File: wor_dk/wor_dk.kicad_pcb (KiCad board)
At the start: 4 copper layers, 108.7 x 57.5 mm, 139 parts, among them J101 Conn_01x02, J102 Conn_02x03_Odd_Even, J103 Conn_02x03_Odd_Even, J104 Conn_01x02, J201 SWD, J301 SMA, J302 Conn_02x04_Odd_Even, J303 Conn_02x06_Odd_Even, J401 USB_C_Receptacle_USB2.0_16P, J501 SWD, J502 USB_C_Receptacle_USB2.0_16P, J503 SWD, Q501 BSS84, SW201 SW_Push, SW501 SW_Push, U201 nRF52840, U202 TMUX1112PWR, U203 TMUX1112PWR, U301 Si4467, U401 FT232RL, U501 TLV1117-33, U502 LPC11U35FHI33_501, Y201 32.768kHz, Y202 32MHz, Y301 26MHz, Y501 12MHz

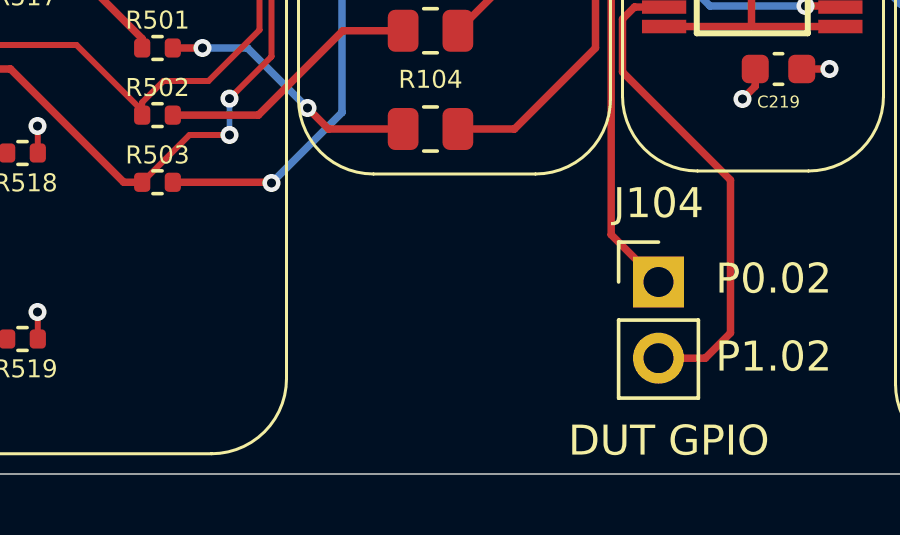
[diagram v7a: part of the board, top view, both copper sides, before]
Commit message: wor_dk: PCB: add smart tulip logo
This also requires the logos library to be added, so that we don't get
a DRC warning.
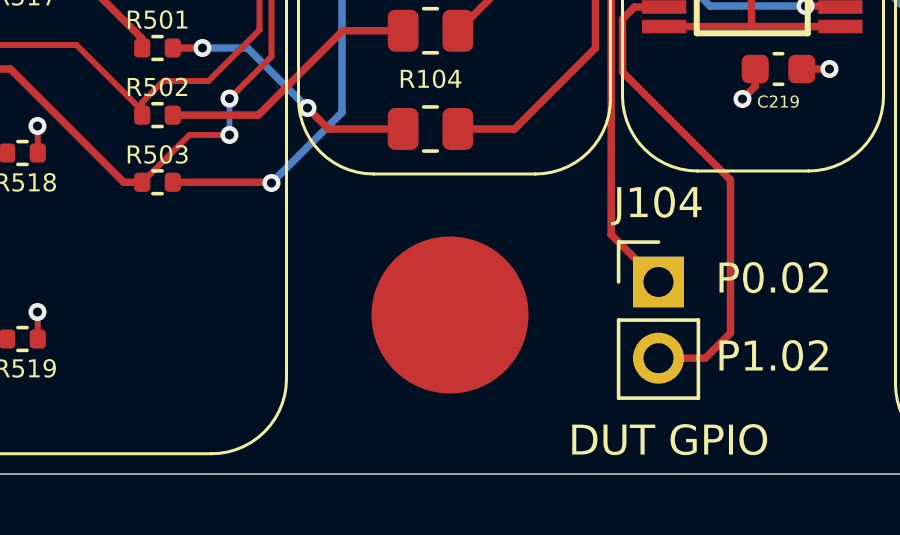
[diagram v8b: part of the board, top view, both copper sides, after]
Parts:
- added G1: smart logo, Logos:smart_tulip_soldermask, F.Cu at (102.1, 106.8)
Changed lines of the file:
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@@
 		)
 	)
+	(footprint "Logos:smart_tulip_soldermask"
+		(layer "F.Cu")
+		(at 102.13 106.85)
+		(property "Reference" "G1"
+			(at -1.016 -3.302 0)
+			(layer "F.SilkS")
+			(hide yes)
+			(effects
+				(font
+					(size 0.4 0.4)
+					(thickness 0.1)
+				)
+			)
+		)
+		(property "Value" "smart logo"
+			(at 0.254 3.556 0)
+			(layer "F.SilkS")
+			(hide yes)
+			(effects
+				(font
+					(size 1.524 1.524)
+					(thickness 0.3)
+				)
+			)
+		)
+		(property "Footprint" "Logos:smart_tulip_soldermask"
+			(at 0 0 0)
+			(unlocked yes)
+			(layer "F.Fab")
+			(hide yes)
+			(effects
+				(font
+					(size 1.27 1.27)
+					(thickness 0.15)
+				)
+			)
+		)
+		(property "Datasheet" ""
+			(at 0 0 0)
+			(unlocked yes)
+			(layer "F.Fab")
+			(hide yes)
+			(effects
+				(font
+					(size 1.27 1.27)
+					(thickness 0.15)
+				)
+			)
+		)
+		(property "Description" ""
+			(at 0 0 0)
+			(unlocked yes)
+			(layer "F.Fab")
+			(hide yes)
+			(effects
+				(font
+					(size 1.27 1.27)
+					(thickness 0.15)
+				)
+			)
+		)
+		(attr through_hole board_only)
+		(fp_poly
+			(pts
+				(xy 1.422426 -0.378883) (xy 1.420006 -0.317863) (xy 1.413171 -0.245699) (xy 1.40263 -0.167389) (xy 1.389089 -0.087929)
+				(xy 1.373258 -0.012316) (xy 1.36666 0.014876) (xy 1.315718 0.182018) (xy 1.249879 0.341973) (xy 1.169932 0.493942)
+				(xy 1.076662 0.637125) (xy 0.970857 0.770722) (xy 0.853303 0.893933) (xy 0.724786 1.005959) (xy 0.586095 1.105999)
+				(xy 0.438015 1.193254) (xy 0.281333 1.266924) (xy 0.116836 1.326208) (xy 0.060618 1.342576) (xy -0.004628 1.358579)
+				(xy -0.077678 1.37333) (xy -0.15378 1.386112) (xy -0.22818 1.396206) (xy -0.296128 1.402895) (xy -0.35287 1.40546)
+				(xy -0.355534 1.405467) (xy -0.423333 1.405467) (xy -0.423333 1.120269) (xy -0.309799 1.110728)
+				(xy -0.144538 1.08871) (xy 0.014273 1.051181) (xy 0.166026 0.998503) (xy 0.310111 0.931038) (xy 0.44592 0.849149)
+				(xy 0.572844 0.753198) (xy 0.690273 0.643547) (xy 0.797599 0.520558) (xy 0.883927 0.400481) (xy 0.949311 0.289348)
+				(xy 1.006427 0.169348) (xy 1.053931 0.044301) (xy 1.090479 -0.081973) (xy 1.114728 -0.205651) (xy 1.123001 -0.2794)
+				(xy 1.125741 -0.31275) (xy 1.1284 -0.341175) (xy 1.130439 -0.358949) (xy 1.130574 -0.359833) (xy 1.132569 -0.379718)
+				(xy 1.13384 -0.405692) (xy 1.133905 -0.408516) (xy 1.134534 -0.440266) (xy 1.4224 -0.440266) (xy 1.422426 -0.378883)
+			)
+			(stroke
+				(width 0.01)
+				(type solid)
+			)
+			(fill solid)
+			(layer "F.Mask")
+		)
+		(fp_poly
+			(pts
+				(xy -1.85349 -2.027975) (xy -1.769722 -2.016646) (xy -1.682248 -1.999131) (xy -1.596562 -1.976547)
+				(xy -1.518155 -1.950012) (xy -1.510575 -1.947045) (xy -1.379298 -1.886043) (xy -1.256531 -1.811061)
+				(xy -1.143543 -1.723118) (xy -1.041596 -1.623235) (xy -0.951959 -1.512431) (xy -0.927803 -1.477433)
+				(xy -0.871278 -1.384506) (xy -0.823907 -1.288617) (xy -0.783743 -1.185302) (xy -0.748837 -1.070095)
+				(xy -0.746831 -1.062566) (xy -0.724422 -0.977899) (xy -0.721751 -0.08255) (xy -0.71908 0.812801)
+				(xy -0.768056 0.811532) (xy -0.800202 0.810232) (xy -0.82942 0.808279) (xy -0.842433 0.806954) (xy -0.990098 0.780992)
+				(xy -1.126779 0.742744) (xy -1.253726 0.691629) (xy -1.372188 0.62707) (xy -1.483415 0.548485) (xy -1.577133 0.466475)
+				(xy -1.674185 0.364294) (xy -1.755806 0.258166) (xy -1.823403 0.145898) (xy -1.878387 0.025297)
+				(xy -1.901206 -0.037666) (xy -1.912127 -0.070833) (xy -1.921877 -0.102169) (xy -1.930522 -0.132787)
+				(xy -1.938128 -0.163801) (xy -1.944761 -0.196327) (xy -1.950489 -0.231477) (xy -1.955377 -0.270367)
+				(xy -1.959492 -0.31411) (xy -1.9629 -0.363821) (xy -1.965667 -0.420613) (xy -1.96786 -0.4856) (xy -1.969545 -0.559898)
+				(xy -1.970788 -0.64462) (xy -1.971656 -0.74088) (xy -1.972216 -0.849793) (xy -1.972533 -0.972472)
+				(xy -1.972673 -1.110032) (xy -1.972704 -1.238249) (xy -1.972733 -2.031999) (xy -1.928061 -2.031999)
+				(xy -1.85349 -2.027975)
+			)
+			(stroke
+				(width 0.01)
+				(type solid)
+			)
+			(fill solid)
+			(layer "F.Mask")
+		)
+		(fp_poly
+			(pts
+				(xy 2.014986 -0.366183) (xy 2.013367 -0.31459) (xy 2.008961 -0.251486) (xy 2.002299 -0.181965) (xy 1.993912 -0.111119)
+				(xy 1.984331 -0.044044) (xy 1.976816 0) (xy 1.935403 0.181311) (xy 1.879264 0.361862) (xy 1.809646 0.538651)
+				(xy 1.727793 0.708674) (xy 1.634954 0.868926) (xy 1.585094 0.944034) (xy 1.470967 1.094835) (xy 1.343369 1.238976)
+				(xy 1.205012 1.373744) (xy 1.058608 1.496427) (xy 0.960967 1.568023) (xy 0.79508 1.672971) (xy 0.620613 1.76425)
+				(xy 0.439187 1.841309) (xy 0.252427 1.9036) (xy 0.061957 1.950573) (xy -0.130601 1.981678) (xy -0.30198 1.995552)
+				(xy -0.423333 2.00071) (xy -0.423333 1.710267) (xy -0.38735 1.709061) (xy -0.355963 1.707714) (xy -0.325689 1.705975)
+				(xy -0.321733 1.705697) (xy -0.298943 1.70403) (xy -0.265806 1.701596) (xy -0.22886 1.698876) (xy -0.222757 1.698426)
+				(xy -0.163102 1.692069) (xy -0.092387 1.681375) (xy -0.015635 1.667305) (xy 0.062131 1.650822) (xy 0.135888 1.632889)
+				(xy 0.174258 1.622373) (xy 0.35114 1.562729) (xy 0.521412 1.487915) (xy 0.684146 1.398713) (xy 0.838412 1.295908)
+				(xy 0.983279 1.180282) (xy 1.117817 1.052617) (xy 1.241096 0.913697) (xy 1.352187 0.764304) (xy 1.450159 0.605221)
+				(xy 1.503078 0.503767) (xy 1.54518 0.414252) (xy 1.57972 0.333112) (xy 1.608782 0.254802) (xy 1.634449 0.17378)
+				(xy 1.654635 0.100626) (xy 1.674989 0.012869) (xy 1.69305 -0.084114) (xy 1.70803 -0.184701) (xy 1.719138 -0.283274)
+				(xy 1.725584 -0.37421) (xy 1.726779 -0.412749) (xy 1.7272 -0.440266) (xy 2.015067 -0.440266) (xy 2.014986 -0.366183)
+			)
+			(stroke
+				(width 0.01)
+				(type solid)
+			)
+			(fill solid)
+			(layer "F.Mask")
+		)
+		(fp_poly
+			(pts
+				(xy 0.82913 -1.197212) (xy 0.828938 -1.051014) (xy 0.828674 -0.920675) (xy 0.828303 -0.805123) (xy 0.827792 -0.703284)
+				(xy 0.827106 -0.614085) (xy 0.826211 -0.536453) (xy 0.825073 -0.469313) (xy 0.823656 -0.411592)
+				(xy 0.821928 -0.362218) (xy 0.819853 -0.320117) (xy 0.817398 -0.284215) (xy 0.814527 -0.253439)
+				(xy 0.811207 -0.226716) (xy 0.807404 -0.202971) (xy 0.803082 -0.181133) (xy 0.798209 -0.160127)
+				(xy 0.795662 -0.150022) (xy 0.751166 -0.008914) (xy 0.692897 0.123628) (xy 0.621745 0.24685) (xy 0.538601 0.359998)
+				(xy 0.444358 0.46232) (xy 0.339904 0.553059) (xy 0.226133 0.631464) (xy 0.103934 0.696779) (xy -0.0258 0.748252)
+				(xy -0.16218 0.785127) (xy -0.304314 0.806652) (xy -0.338272 0.809389) (xy -0.423996 0.815157) (xy -0.421494 0.054617)
+				(xy -0.145595 0.054617) (xy -0.142333 0.117536) (xy -0.12428 0.17979) (xy -0.101945 0.222459) (xy -0.066009 0.265527)
+				(xy -0.017982 0.303008) (xy 0.037405 0.331249) (xy 0.040617 0.33248) (xy 0.085559 0.342776) (xy 0.13803 0.344634)
+				(xy 0.191058 0.338358) (xy 0.237669 0.324251) (xy 0.238555 0.323862) (xy 0.288476 0.293885) (xy 0.333949 0.252032)
+				(xy 0.369809 0.203341) (xy 0.378249 0.187477) (xy 0.395458 0.136568) (xy 0.402768 0.079669) (xy 0.400029 0.022884)
+				(xy 0.387087 -0.027682) (xy 0.383801 -0.035354) (xy 0.355383 -0.082238) (xy 0.316327 -0.126594)
+				(xy 0.272052 -0.162732) (xy 0.250107 -0.17571) (xy 0.196331 -0.194824) (xy 0.136072 -0.202465) (xy 0.075585 -0.198312)
+				(xy 0.032622 -0.186812) (xy -0.026355 -0.156201) (xy -0.074446 -0.114376) (xy -0.110871 -0.063715)
+				(xy -0.134847 -0.006592) (xy -0.145595 0.054617) (xy -0.421494 0.054617) (xy -0.421074 -0.072905)
+				(xy -0.420619 -0.217041) (xy -0.420218 -0.345333) (xy -0.419813 -0.45887) (xy -0.419347 -0.558742)
+				(xy -0.418762 -0.646038) (xy -0.418 -0.721847) (xy -0.417003 -0.787257) (xy -0.415713 -0.843359)
+				(xy -0.414074 -0.891241) (xy -0.412026 -0.931993) (xy -0.409513 -0.966703) (xy -0.406476 -0.996461)
+				(xy -0.402858 -1.022356) (xy -0.398601 -1.045478) (xy -0.393647 -1.066914) (xy -0.387938 -1.087756)
+				(xy -0.381417 -1.10909) (xy -0.374026 -1.132008) (xy -0.365707 -1.157597) (xy -0.363117 -1.165661)
+				(xy -0.312441 -1.29833) (xy -0.247887 -1.422165) (xy -0.168826 -1.538156) (xy -0.074631 -1.647294)
+				(xy -0.02822 -1.693406) (xy 0.051789 -1.763811) (xy 0.133435 -1.823452) (xy 0.223172 -1.876869)
+				(xy 0.25976 -1.895985) (xy 0.390025 -1.953105) (xy 0.52452 -1.995111) (xy 0.660861 -2.021344) (xy 0.741299 -2.029162)
+				(xy 0.830039 -2.03459) (xy 0.82913 -1.197212)
+			)
+			(stroke
+				(width 0.01)
+				(type solid)
+			)
+			(fill solid)
+			(layer "F.Mask")
+		)
+		(fp_circle
+			(center -0.3 -0.367509)
+			(end -2.538398 0.75)
+			(stroke
+				(width 0.05)
+				(type default)
+			)
+			(fill none)
+			(layer "F.CrtYd")
+		)
+	)
 	(footprint "Resistor_SMD:R_0402_1005Metric"
 		(layer "F.Cu")
@@
 		)
 	)
+	(gr_circle
+		(center 101.75 106.5)
+		(end 104.267538 106.5)
+		(stroke
+			(width 0.2)
+			(type solid)
+		)
+		(fill solid)
+		(layer "F.Cu")
+	)
 	(gr_arc
